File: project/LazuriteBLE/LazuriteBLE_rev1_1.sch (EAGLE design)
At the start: 22 parts

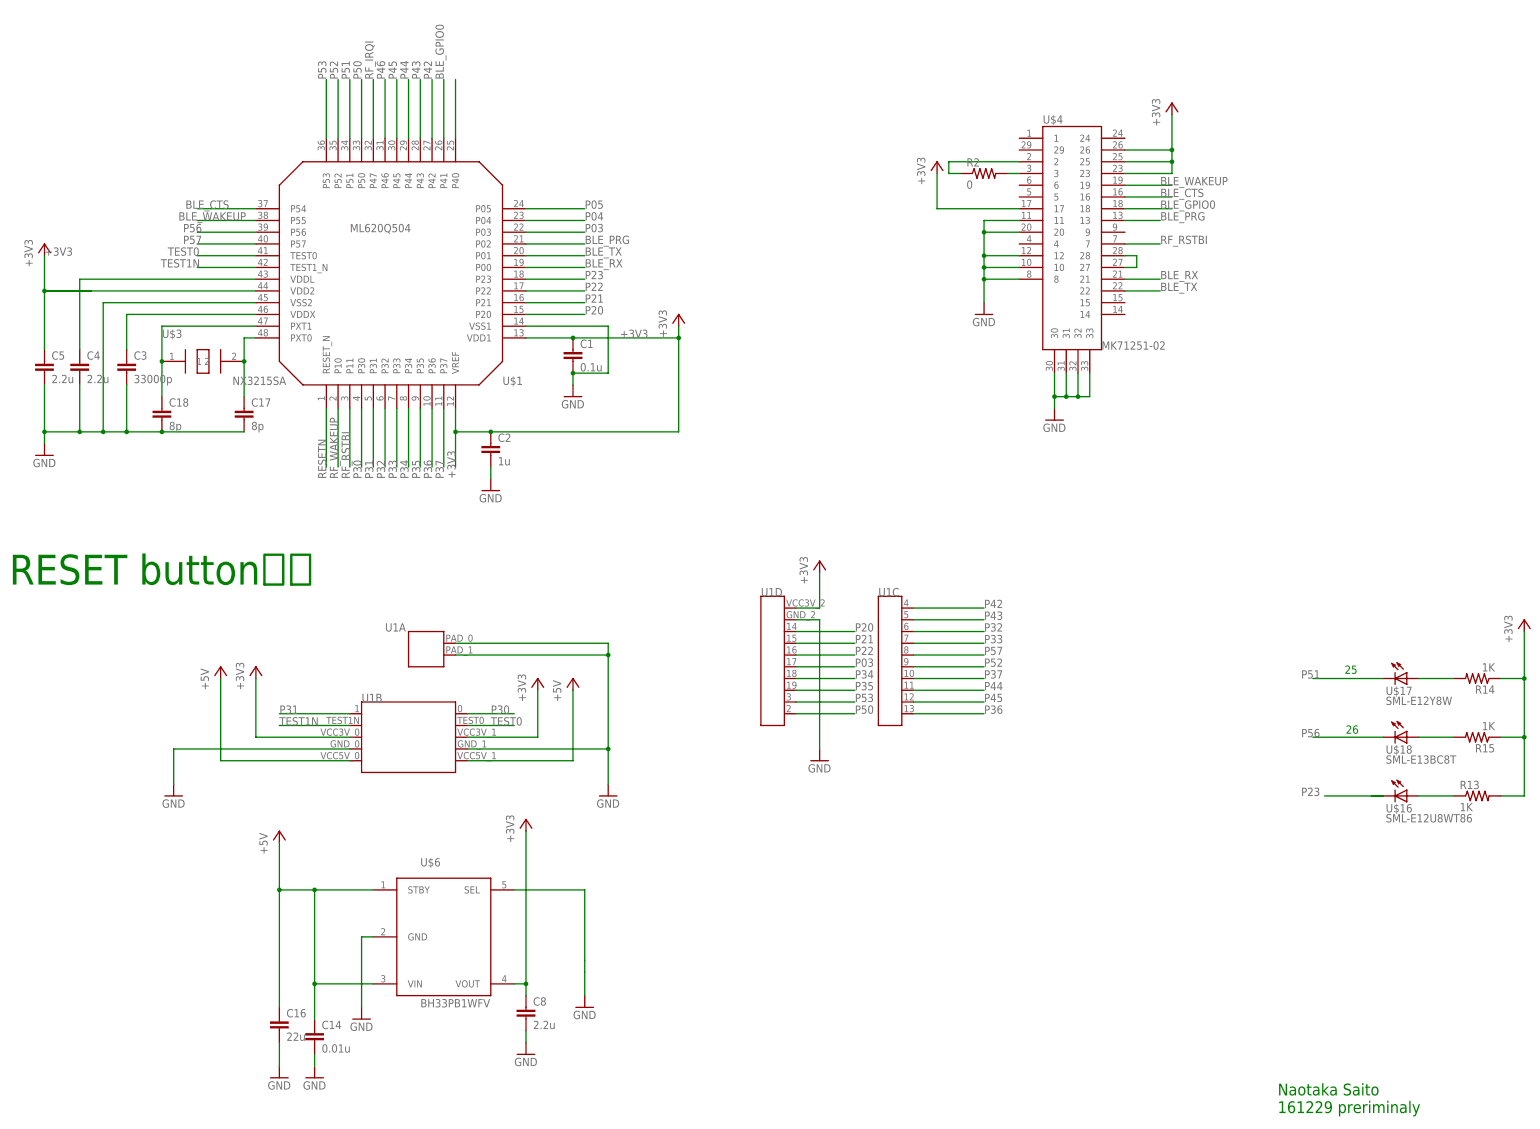
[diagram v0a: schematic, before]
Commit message: modify lazurite ble  - add reset button.
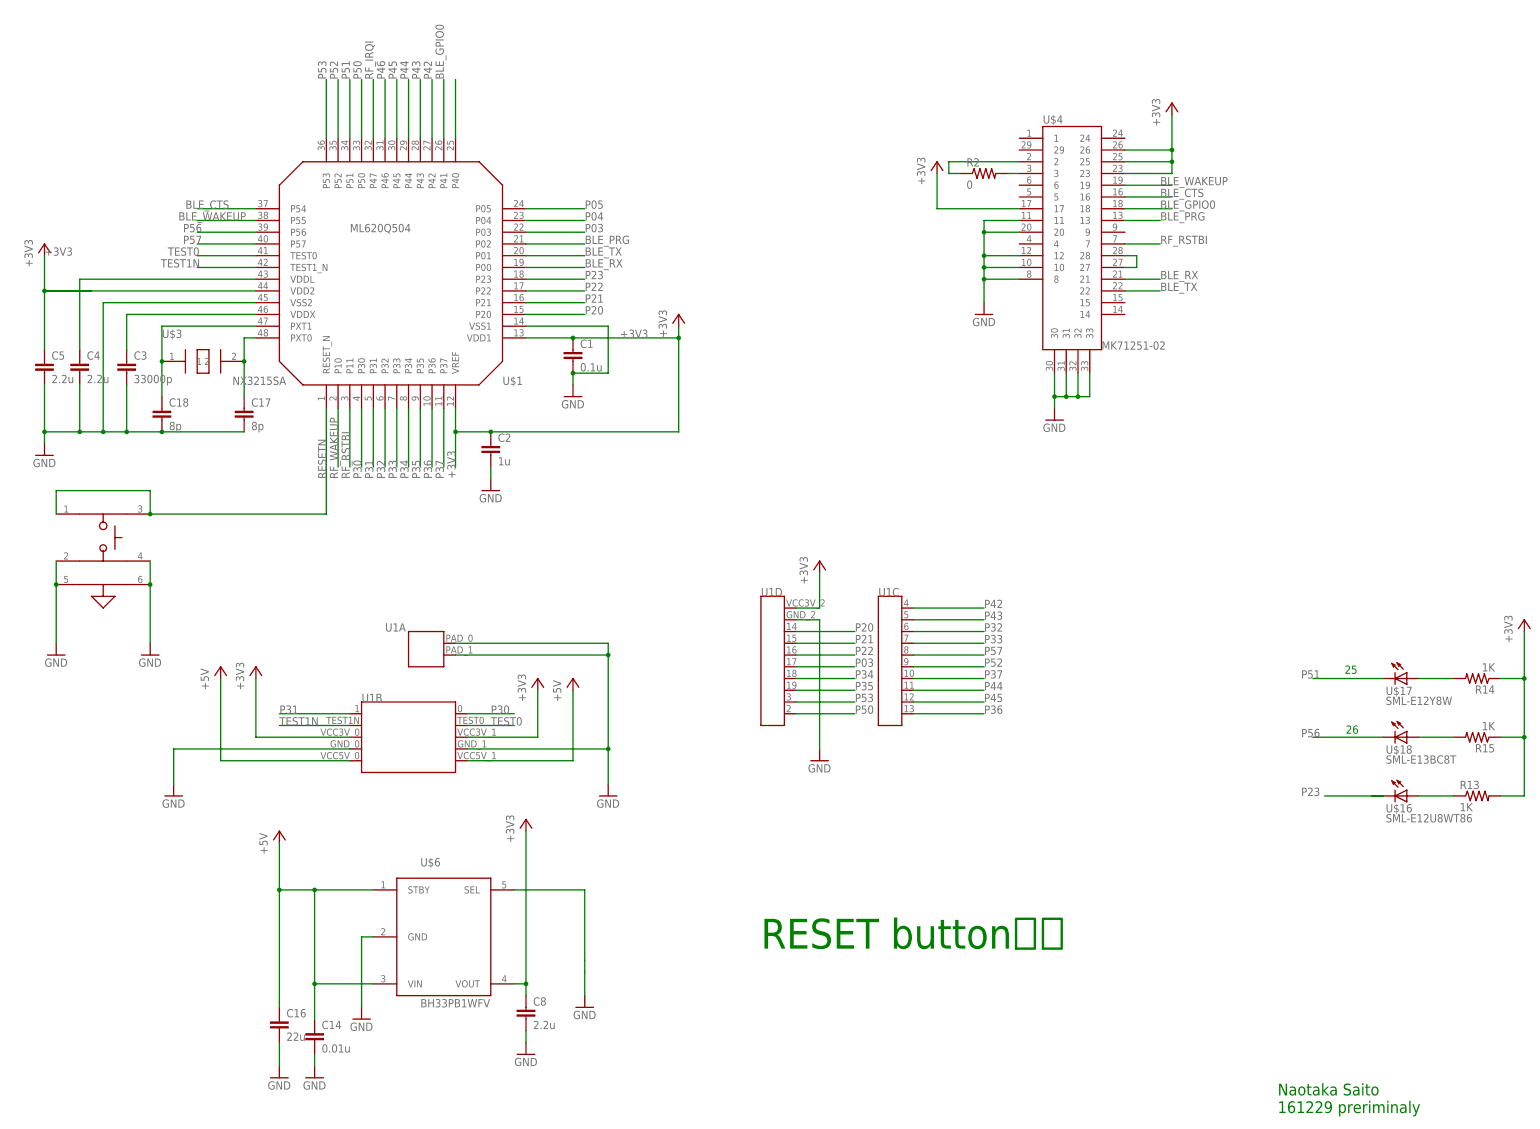
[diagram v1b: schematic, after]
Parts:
- added SW1: SKSGACE010, lz-shield:SKSGACE010
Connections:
- net GND: now also SW1.2, SW1.4, SW1.5, SW1.6
- net RESETN: now also SW1.1, SW1.3
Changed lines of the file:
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@@
 <part name="GND19" library="supply1" deviceset="GND" device=""/>
 <part name="C16" library="rcl" deviceset="C-EU" device="C1206" value="22u"/>
+<part name="SW1" library="lz-shield" deviceset="SKSGACE010" device=""/>
+<part name="GND12" library="supply1" deviceset="GND" device=""/>
+<part name="GND13" library="supply1" deviceset="GND" device=""/>
 </parts>
 <sheets>
@@
 <text x="294.64" y="10.16" size="2.54" layer="91" font="vector">Naotaka Saito
 161229 preriminaly</text>
-<text x="20.32" y="124.46" size="6.4516" layer="91">RESET button追加</text>
+<text x="182.88" y="45.72" size="6.4516" layer="91">RESET button追加</text>
 </plain>
 <instances>
@@
 <instance part="GND19" gate="1" x="78.74" y="17.78"/>
 <instance part="C16" gate="G$1" x="78.74" y="30.48"/>
+<instance part="SW1" gate="G$1" x="40.64" y="134.62"/>
+<instance part="GND12" gate="1" x="50.8" y="109.22"/>
+<instance part="GND13" gate="1" x="30.48" y="109.22"/>
 </instances>
 <busses>
@@
 <pinref part="C16" gate="G$1" pin="2"/>
 </segment>
+<segment>
+<pinref part="SW1" gate="G$1" pin="4"/>
+<wire x1="50.8" y1="129.54" x2="50.8" y2="124.46" width="0.1524" layer="91"/>
+<pinref part="GND12" gate="1" pin="GND"/>
+<pinref part="SW1" gate="G$1" pin="6"/>
+<junction x="50.8" y="124.46"/>
+<wire x1="50.8" y1="124.46" x2="50.8" y2="111.76" width="0.1524" layer="91"/>
+</segment>
+<segment>
+<pinref part="SW1" gate="G$1" pin="2"/>
+<pinref part="SW1" gate="G$1" pin="5"/>
+<wire x1="30.48" y1="129.54" x2="30.48" y2="124.46" width="0.1524" layer="91"/>
+<pinref part="GND13" gate="1" pin="GND"/>
+<wire x1="30.48" y1="124.46" x2="30.48" y2="111.76" width="0.1524" layer="91"/>
+<junction x="30.48" y="124.46"/>
+</segment>
 </net>
 <net name="P04" class="0">
@@
 <net name="RESETN" class="0">
 <segment>
-<wire x1="88.9" y1="162.56" x2="88.9" y2="149.86" width="0.1524" layer="91"/>
+<wire x1="88.9" y1="162.56" x2="88.9" y2="139.7" width="0.1524" layer="91"/>
 <label x="88.9" y="147.32" size="1.778" layer="95" font="vector" rot="R90"/>
 <pinref part="U$1" gate="G$1" pin="RESET_N"/>
-</segment>
-</net>
+<pinref part="SW1" gate="G$1" pin="3"/>
+<wire x1="50.8" y1="139.7" x2="88.9" y2="139.7" width="0.1524" layer="91"/>
+<pinref part="SW1" gate="G$1" pin="1"/>
+<wire x1="30.48" y1="139.7" x2="30.48" y2="144.78" width="0.1524" layer="91"/>
+<wire x1="30.48" y1="144.78" x2="50.8" y2="144.78" width="0.1524" layer="91"/>
+<wire x1="50.8" y1="144.78" x2="50.8" y2="139.7" width="0.1524" layer="91"/>
+<junction x="50.8" y="139.7"/>
+</segment>
+</net>
